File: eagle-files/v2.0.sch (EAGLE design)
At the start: 26 parts, among them U1 MLX90614_

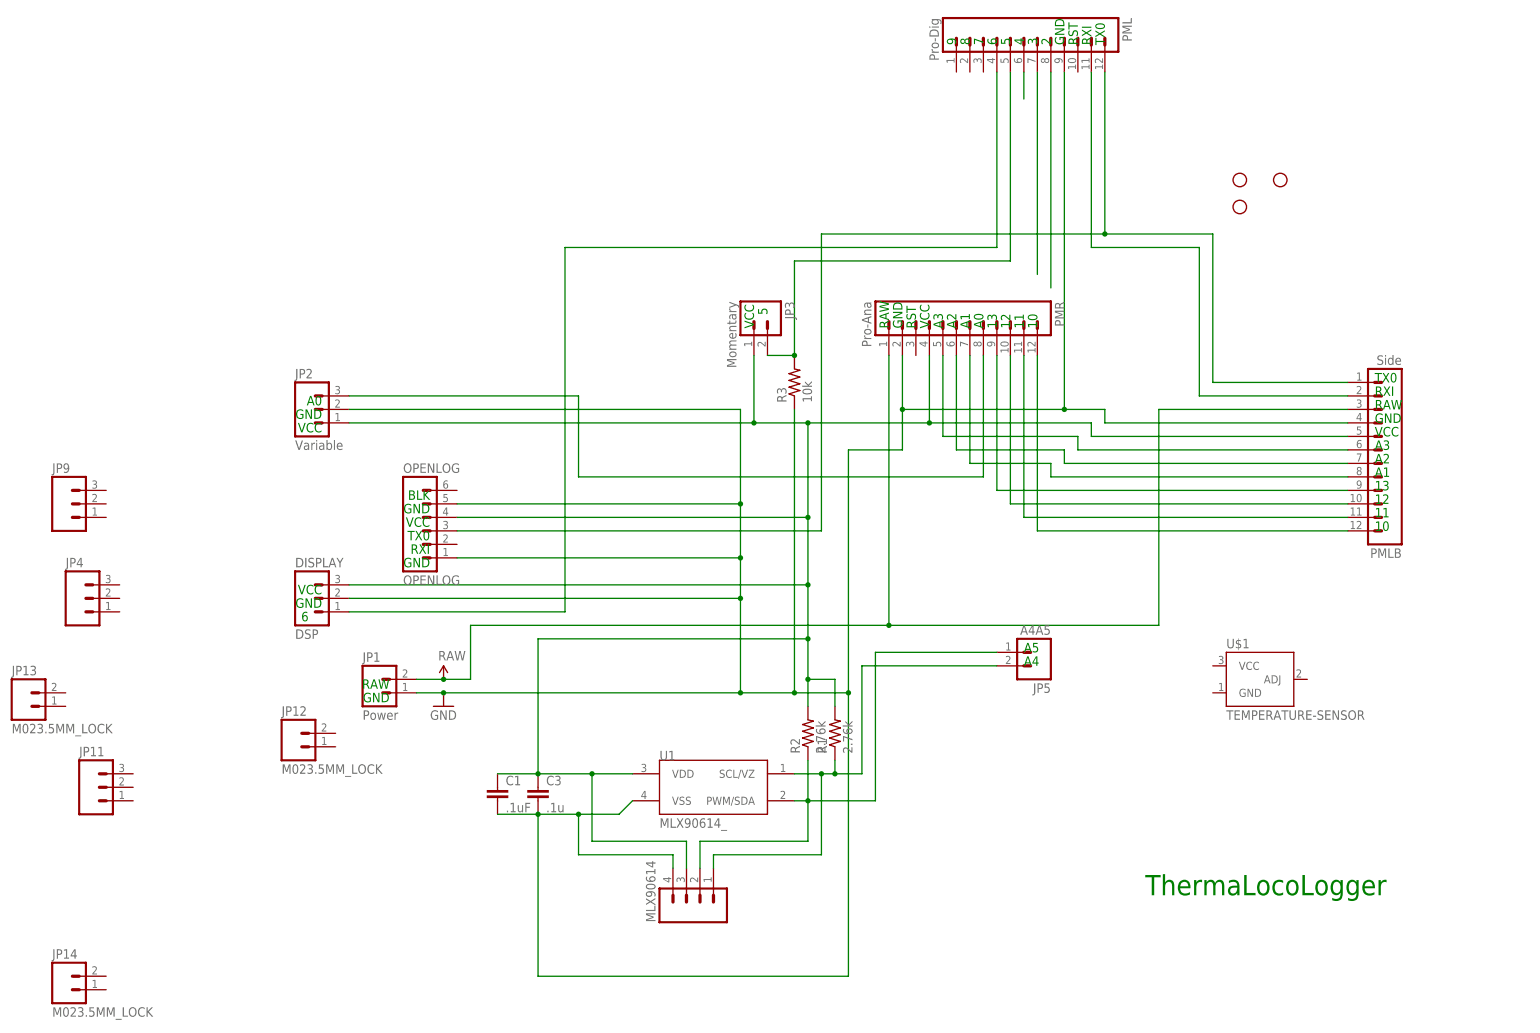
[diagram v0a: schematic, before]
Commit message: Added all parts to schematic
Added all the bits and pieces needed to the shcematic and did a rough
auto route on the board. This is still assuming that the wheel only
needs 4 pins (power, ground, data1, data2). There is no circuit for
clean reading for the wheel yet. Have not run DRC or ERC.
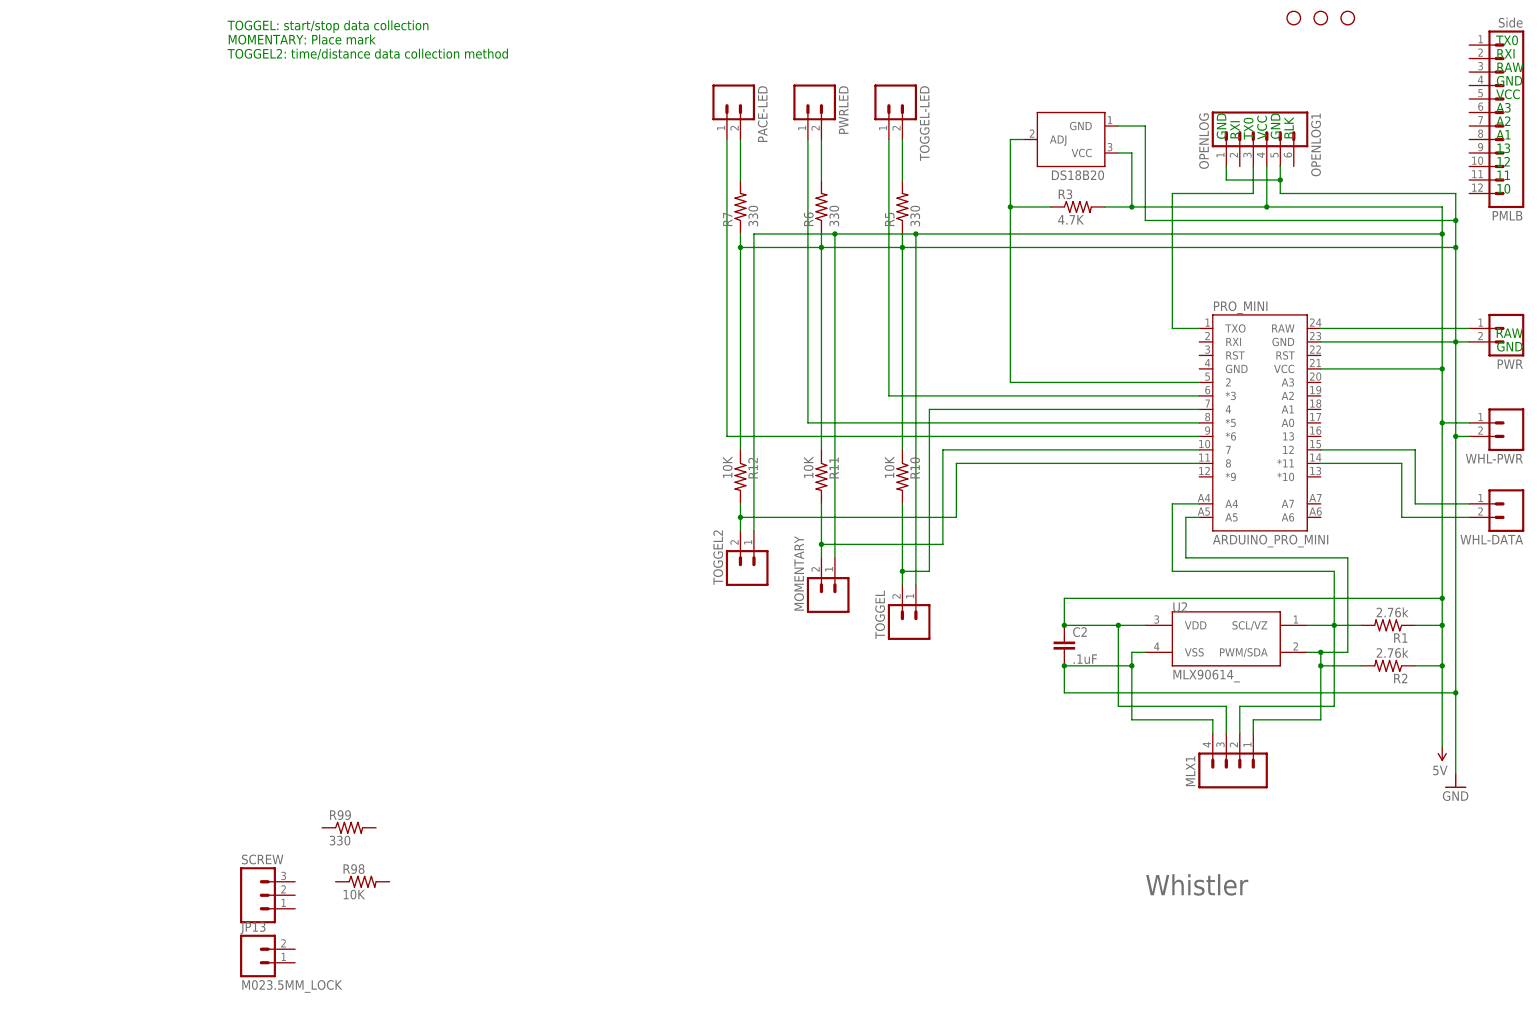
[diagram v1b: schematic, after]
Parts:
- removed C1: .1uF, SparkFun:CAPPTH
- removed C3: .1u, SparkFun:CAPPTH1
- removed DISPLAY: DSP, SparkFun:M03SCREW_LOCK
- removed JP1: Power, SparkFun:M02JST-PTH-2
- removed JP11, JP4, JP9: (no value), SparkFun-Connectors:M03SCREW_LOCK
- removed JP12, JP14: M023.5MM_LOCK, SparkFun-Connectors:M023.5MM_LOCK
- removed JP2: Variable, SparkFun:M03SCREW_LOCK
- removed JP3: Momentary, SparkFun:M02JST-PTH-2
- removed JP5: A4A5, SparkFun:M02PTH
- removed MLX90614: (no value), SparkFun-Connectors:M04SMD2
- removed OPENLOG: OPENLOG, SparkFun:M06LOCK
- removed PML: Pro-Dig, SparkFun:M12PTH
- removed PMR: Pro-Ana, SparkFun:M12PTH
- removed U$1: TEMPERATURE-SENSOR, SparkFun-Sensors:TEMPERATURE-SENSOR
- removed U1: MLX90614_, SparkFun:MLX90614_
- added C2: .1uF, SparkFun-Capacitors:0.1UF-50V-20%(PTH)KIT-EZ
- added DS18B20: TEMPERATURE-SENSOR, SparkFun-Sensors:TEMPERATURE-SENSOR
- added MLX1: (no value), SparkFun-Connectors:M04SMD2
- added MOMENTARY, PACE-LED, PWR, PWRLED, TOGGEL, TOGGEL-LED, TOGGEL2, WHL-DATA, WHL-PWR: M023.5MM_LOCK, SparkFun-Connectors:M023.5MM_LOCK
- added OPENLOG1: OPENLOG, SparkFun:M06LOCK
- added PRO_MINI: ARDUINO_PRO_MINI, SparkFun-Boards:ARDUINO_PRO_MINI
- added R10, R11, R12, R98: 10K, SparkFun-Resistors:10KOHM1/10W1%(0603)0603
- added R5, R6, R7, R99: 330, SparkFun-Resistors:330OHM1/10W1%(0603)
- added SCREW: (no value), SparkFun-Connectors:M03SCREW_LOCK
- added U2: MLX90614_, SparkFun:MLX90614_
- R3: value 10k -> 4.7K
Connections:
- removed net N$16: C1.1, C3.1, DISPLAY.3, JP2.1, JP3.1, MLX90614.3, OPENLOG.4, PMLB.5, PMR.4, R1.2, R2.2, U1.VDD
- removed net N$20: PML.8
- removed net N$21: PML.7
- removed net N$22: PML.6
- removed net SENSOR: JP5.2, MLX90614.1, R1.1, U1.SCL/VZ
- removed net VCC: JP1.2, PMLB.3, PMR.1
- new net 5V: C2.1, DS18B20.VCC, MLX1.3, MOMENTARY.1, OPENLOG1.4, PRO_MINI.VCC, R1.1, R2.1, R3.2, TOGGEL.1, TOGGEL2.1, U2.VDD, WHL-PWR.1
- new net N$1: PRO_MINI.4, R10.2, TOGGEL.2
- new net N$18: PRO_MINI.8, R12.2, TOGGEL2.2
- new net N$7: MLX1.1, PRO_MINI.A5, R2.2, U2.PWM/SDA
- net GND: now also C2.2, DS18B20.GND, MLX1.4, OPENLOG1.1, OPENLOG1.5, PRO_MINI.GND@2, PWR.2, R10.1, R11.1, R12.1, R5.1, R6.1, R7.1, U2.VSS, WHL-PWR.2; no longer C1.2, C3.2, DISPLAY.2, JP1.1, JP2.2, MLX90614.4, OPENLOG.1, OPENLOG.5, PML.9, PMLB.4, PMR.2, R3.1, U1.VSS
- net N$10: now also MOMENTARY.2, PRO_MINI.7, R11.2; no longer PMLB.11, PMR.11
- net N$11: now also PRO_MINI.*11, WHL-DATA.2; no longer PMLB.10, PMR.10
- net N$12: now also PRO_MINI.*3, TOGGEL-LED.1; no longer PMLB.9, PMR.9
- net N$13: now also PACE-LED.1, PRO_MINI.*6; no longer PMLB.8, PMR.7
- net N$14: now also PWRLED.2, R6.2; no longer PMLB.7, PMR.6
- net N$15: now also PACE-LED.2, R7.2; no longer PMLB.6, PMR.5
- net N$2: now also DS18B20.ADJ, PRO_MINI.2, R3.1; no longer JP5.1, MLX90614.2, R2.1, U1.PWM/SDA
- net N$3: now also PRO_MINI.12, WHL-DATA.1; no longer JP3.2, PML.5, R3.2
- net N$4: now also PRO_MINI.RAW, PWR.1; no longer DISPLAY.1, PML.4
- net N$5: now also R5.2, TOGGEL-LED.2; no longer JP2.3, PMR.8
- net N$6: now also PRO_MINI.*5, PWRLED.1; no longer OPENLOG.3, PML.12, PMLB.1
- net N$8: now also OPENLOG1.3, PRO_MINI.TXO; no longer PML.11, PMLB.2
- net N$9: now also MLX1.2, PRO_MINI.A4, R1.2, U2.SCL/VZ; no longer PMLB.12, PMR.12
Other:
- note added: "TOGGEL: start/stop data collection MOMENTARY: Place mark TOGGEL2: time/distance data collection method"
- note added: "Whistler"
- note removed: "2"
- note removed: "3"
- note removed: "4"
- note removed: "5"
- note removed: "6"
- note removed: "7"
- note removed: "8"
- note removed: "9"
- note removed: "A0"
- note removed: "A4"
- note removed: "A5"
- note removed: "RST"
- note removed: "ThermaLocoLogger"
- moved on the sheet: JP13, PMLB, R1, R2, R3

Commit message: added a few new compnents
Added compnents and the ground plane. Looking at breaking out the reset
button, but the pins are all blocked.
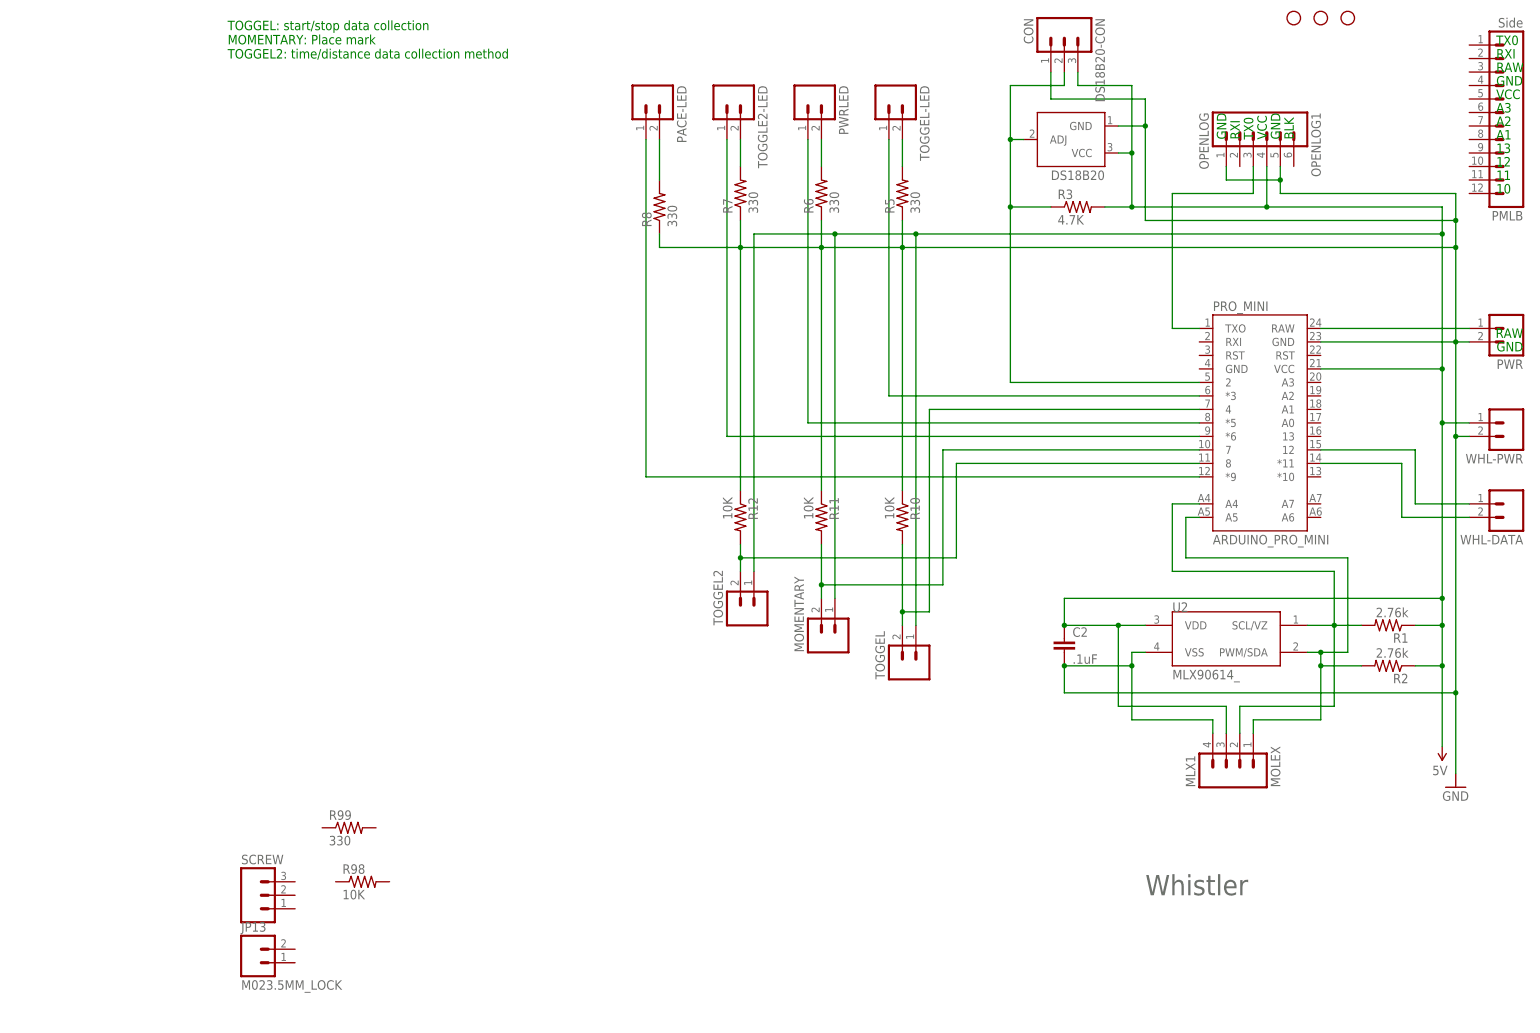
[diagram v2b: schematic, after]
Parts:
- added DS18B20-CON: CON, SparkFun-Connectors:M03SCREW_LOCK
- added R8: 330, SparkFun-Resistors:330OHM1/10W1%(0603)
- added TOGGLE2-LED: M023.5MM_LOCK, SparkFun-Connectors:M023.5MM_LOCK
- MLX1: value (none) -> MOLEX
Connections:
- new net N$16: PACE-LED.2, R8.2
- new net N$17: PACE-LED.1, PRO_MINI.*9
- net 5V: now also DS18B20-CON.3
- net GND: now also DS18B20-CON.1, R8.1
- net N$13: now also TOGGLE2-LED.1; no longer PACE-LED.1
- net N$15: now also TOGGLE2-LED.2; no longer PACE-LED.2
- net N$2: now also DS18B20-CON.2
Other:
- moved on the sheet: MOMENTARY, PACE-LED, R10, R11, R12, R5, R6, R7, TOGGEL, TOGGEL2
